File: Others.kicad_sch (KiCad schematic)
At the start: 18 parts, among them J15 UFL, J16 IO1, J17 IO2, Q14 SI2312BDS

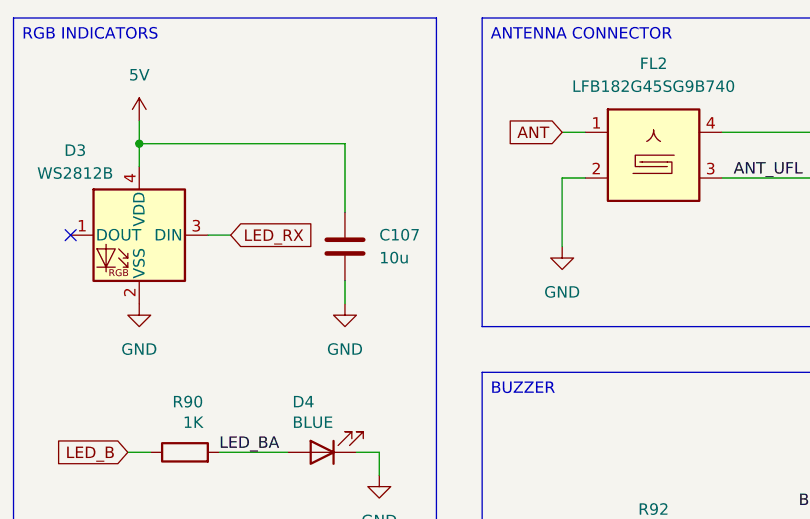
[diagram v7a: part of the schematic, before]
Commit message: IMU filtering and layout
Added a missing capacitor for the IMU.
Updated the PCB layout.
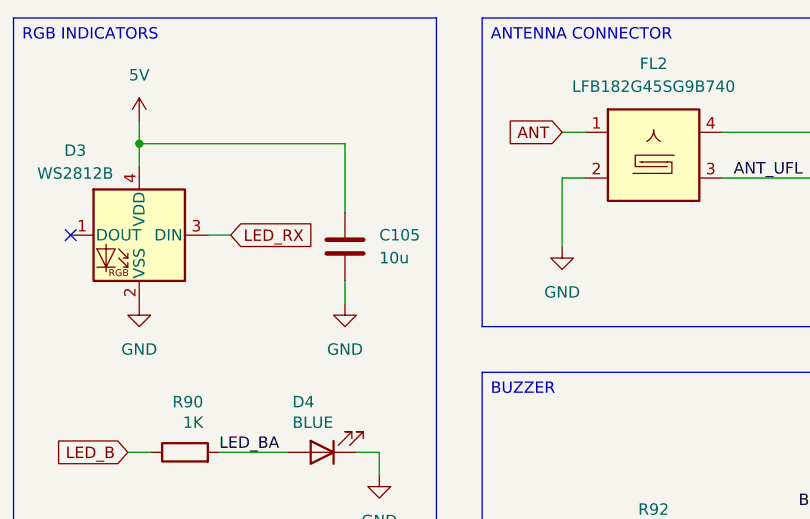
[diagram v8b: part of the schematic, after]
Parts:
- renumbered C107 to C105
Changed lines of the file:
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@@
 		(on_board yes)
 		(dnp no)
-		(property "Reference" "#PWR0215"
+		(property "Reference" "#PWR0216"
 			(at 111.76 96.52 0)
 			(effects
@@
 			(project "ThunderHorse"
 				(path "/ac187c6c-fa53-41cc-bce1-6f39a42a92e8/111cf19a-e0f8-4ba5-b5cb-1102d2b05aed"
-					(reference "#PWR0215")
+					(reference "#PWR0216")
 					(unit 1)
 				)
@@
 		(dnp no)
 		(fields_autoplaced yes)
-		(property "Reference" "#PWR0218"
+		(property "Reference" "#PWR0219"
 			(at 151.13 116.84 0)
 			(effects
@@
 			(project "ThunderHorse"
 				(path "/ac187c6c-fa53-41cc-bce1-6f39a42a92e8/111cf19a-e0f8-4ba5-b5cb-1102d2b05aed"
-					(reference "#PWR0218")
+					(reference "#PWR0219")
 					(unit 1)
 				)
@@
 		(dnp no)
 		(fields_autoplaced yes)
-		(property "Reference" "#PWR0213"
+		(property "Reference" "#PWR0214"
 			(at 85.09 77.47 0)
 			(effects
@@
 			(project "ThunderHorse"
 				(path "/ac187c6c-fa53-41cc-bce1-6f39a42a92e8/111cf19a-e0f8-4ba5-b5cb-1102d2b05aed"
-					(reference "#PWR0213")
+					(reference "#PWR0214")
 					(unit 1)
 				)
@@
 		(dnp no)
 		(fields_autoplaced yes)
-		(property "Reference" "#PWR0221"
+		(property "Reference" "#PWR0222"
 			(at 165.1 71.12 0)
 			(effects
@@
 			(project "ThunderHorse"
 				(path "/ac187c6c-fa53-41cc-bce1-6f39a42a92e8/111cf19a-e0f8-4ba5-b5cb-1102d2b05aed"
-					(reference "#PWR0221")
+					(reference "#PWR0222")
 					(unit 1)
 				)
@@
 		(dnp no)
 		(fields_autoplaced yes)
-		(property "Reference" "#PWR0227"
+		(property "Reference" "#PWR0228"
 			(at 217.17 57.15 0)
 			(effects
@@
 			(project "ThunderHorse"
 				(path "/ac187c6c-fa53-41cc-bce1-6f39a42a92e8/111cf19a-e0f8-4ba5-b5cb-1102d2b05aed"
-					(reference "#PWR0227")
+					(reference "#PWR0228")
 					(unit 1)
 				)
@@
 		(on_board yes)
 		(dnp no)
-		(property "Reference" "#PWR0216"
+		(property "Reference" "#PWR0217"
 			(at 111.76 114.3 0)
 			(effects
@@
 			(project "ThunderHorse"
 				(path "/ac187c6c-fa53-41cc-bce1-6f39a42a92e8/111cf19a-e0f8-4ba5-b5cb-1102d2b05aed"
-					(reference "#PWR0216")
+					(reference "#PWR0217")
 					(unit 1)
 				)
@@
 		(dnp no)
 		(fields_autoplaced yes)
-		(property "Reference" "#PWR0217"
+		(property "Reference" "#PWR0218"
 			(at 132.08 71.12 0)
 			(effects
@@
 			(project "ThunderHorse"
 				(path "/ac187c6c-fa53-41cc-bce1-6f39a42a92e8/111cf19a-e0f8-4ba5-b5cb-1102d2b05aed"
-					(reference "#PWR0217")
+					(reference "#PWR0218")
 					(unit 1)
 				)
@@
 		(on_board yes)
 		(dnp no)
-		(property "Reference" "#PWR0212"
+		(property "Reference" "#PWR0213"
 			(at 85.09 54.61 0)
 			(effects
@@
 			(project "ThunderHorse"
 				(path "/ac187c6c-fa53-41cc-bce1-6f39a42a92e8/111cf19a-e0f8-4ba5-b5cb-1102d2b05aed"
-					(reference "#PWR0212")
+					(reference "#PWR0213")
 					(unit 1)
 				)
@@
 		(dnp no)
 		(fields_autoplaced yes)
-		(property "Reference" "#PWR0222"
+		(property "Reference" "#PWR0223"
 			(at 173.99 71.12 0)
 			(effects
@@
 			(project "ThunderHorse"
 				(path "/ac187c6c-fa53-41cc-bce1-6f39a42a92e8/111cf19a-e0f8-4ba5-b5cb-1102d2b05aed"
-					(reference "#PWR0222")
+					(reference "#PWR0223")
 					(unit 1)
 				)
@@
 		(dnp no)
 		(fields_autoplaced yes)
-		(property "Reference" "#PWR0214"
+		(property "Reference" "#PWR0215"
 			(at 107.95 77.47 0)
 			(effects
@@
 			(project "ThunderHorse"
 				(path "/ac187c6c-fa53-41cc-bce1-6f39a42a92e8/111cf19a-e0f8-4ba5-b5cb-1102d2b05aed"
-					(reference "#PWR0214")
+					(reference "#PWR0215")
 					(unit 1)
 				)
@@
 		(dnp no)
 		(fields_autoplaced yes)
-		(property "Reference" "#PWR0225"
+		(property "Reference" "#PWR0226"
 			(at 213.36 92.71 0)
 			(effects
@@
 			(project "ThunderHorse"
 				(path "/ac187c6c-fa53-41cc-bce1-6f39a42a92e8/111cf19a-e0f8-4ba5-b5cb-1102d2b05aed"
-					(reference "#PWR0225")
+					(reference "#PWR0226")
 					(unit 1)
 				)
@@
 		(dnp no)
 		(fields_autoplaced yes)
-		(property "Reference" "#PWR0219"
+		(property "Reference" "#PWR0220"
 			(at 161.29 91.44 0)
 			(effects
@@
 			(project "ThunderHorse"
 				(path "/ac187c6c-fa53-41cc-bce1-6f39a42a92e8/111cf19a-e0f8-4ba5-b5cb-1102d2b05aed"
-					(reference "#PWR0219")
+					(reference "#PWR0220")
 					(unit 1)
 				)
@@
 		(dnp no)
 		(fields_autoplaced yes)
-		(property "Reference" "#PWR0228"
+		(property "Reference" "#PWR0229"
 			(at 217.17 92.71 0)
 			(effects
@@
 			(project "ThunderHorse"
 				(path "/ac187c6c-fa53-41cc-bce1-6f39a42a92e8/111cf19a-e0f8-4ba5-b5cb-1102d2b05aed"
-					(reference "#PWR0228")
+					(reference "#PWR0229")
 					(unit 1)
 				)
@@
 		(dnp no)
 		(fields_autoplaced yes)
-		(property "Reference" "C107"
+		(property "Reference" "C105"
 			(at 111.76 63.4999 0)
 			(effects
@@
 			(project "ThunderHorse"
 				(path "/ac187c6c-fa53-41cc-bce1-6f39a42a92e8/111cf19a-e0f8-4ba5-b5cb-1102d2b05aed"
-					(reference "C107")
+					(reference "C105")
 					(unit 1)
 				)
@@
 		(dnp no)
 		(fields_autoplaced yes)
-		(property "Reference" "#PWR0220"
+		(property "Reference" "#PWR0221"
 			(at 161.29 116.84 0)
 			(effects
@@
 			(project "ThunderHorse"
 				(path "/ac187c6c-fa53-41cc-bce1-6f39a42a92e8/111cf19a-e0f8-4ba5-b5cb-1102d2b05aed"
-					(reference "#PWR0220")
+					(reference "#PWR0221")
 					(unit 1)
 				)
@@
 		(dnp no)
 		(fields_autoplaced yes)
-		(property "Reference" "#PWR0226"
+		(property "Reference" "#PWR0227"
 			(at 213.36 113.03 0)
 			(effects
@@
 			(project "ThunderHorse"
 				(path "/ac187c6c-fa53-41cc-bce1-6f39a42a92e8/111cf19a-e0f8-4ba5-b5cb-1102d2b05aed"
-					(reference "#PWR0226")
+					(reference "#PWR0227")
 					(unit 1)
 				)
@@
 		(dnp no)
 		(fields_autoplaced yes)
-		(property "Reference" "#PWR0224"
+		(property "Reference" "#PWR0225"
 			(at 213.36 77.47 0)
 			(effects
@@
 			(project "ThunderHorse"
 				(path "/ac187c6c-fa53-41cc-bce1-6f39a42a92e8/111cf19a-e0f8-4ba5-b5cb-1102d2b05aed"
-					(reference "#PWR0224")
+					(reference "#PWR0225")
 					(unit 1)
 				)
@@
 		(dnp no)
 		(fields_autoplaced yes)
-		(property "Reference" "#PWR0223"
+		(property "Reference" "#PWR0224"
 			(at 213.36 57.15 0)
 			(effects
@@
 			(project "ThunderHorse"
 				(path "/ac187c6c-fa53-41cc-bce1-6f39a42a92e8/111cf19a-e0f8-4ba5-b5cb-1102d2b05aed"
-					(reference "#PWR0223")
-					(unit 1)
-				)
+					(reference "#PWR0224")
+					(unit 1)
+				)
